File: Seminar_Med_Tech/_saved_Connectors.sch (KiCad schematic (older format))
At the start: 2 parts

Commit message: Updated Dokumentation
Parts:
- added JP?: Jumper_NC_Dual, symbol Jumper_NC_Dual
- added R?: R, symbol R
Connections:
- net SPI_CLK: now reaches J?.13 (P13)
- net EXT_CLK: now reaches J?.15 (P15)
- net GND: now reaches J?.4 (P4)
- net GND: now also J?.2 (P2), JP?.1
- net SPI_START: now reaches J?.1 (P1)
- net /RESET: now reaches J?.10 (P10)
- net SPI_IN: now reaches J?.12 (P12)
- net SPI_OUT: now reaches J?.14 (P14)
- net at J?.18 (P18): now also JP?.3
- net SPI_CS1: now reaches J?.3 (P3)
- net SPI_DRDY: now reaches J?.5 (P5)
- net SPI_CS2: now reaches J?.7 (P7)
- new net CLKSEL: JP?.2, R?.2
- new net DVDD: R?.1
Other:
- moved on the sheet: J?
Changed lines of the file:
@@
 L CONN_02X10 J?
 U 1 1 593AD152
-P 6150 4000
-F 0 "J?" H 6150 4550 50  0000 C CNN
-F 1 "CONN_02X10" V 6150 4000 50  0000 C CNN
-F 2 "" H 6150 2800 50  0001 C CNN
-F 3 "" H 6150 2800 50  0001 C CNN
-	1    6150 4000
+P 6625 4000
+F 0 "J?" H 6625 4550 50  0000 C CNN
+F 1 "CONN_02X10" V 6625 4000 50  0000 C CNN
+F 2 "" H 6625 2800 50  0001 C CNN
+F 3 "" H 6625 2800 50  0001 C CNN
+	1    6625 4000
 	1    0    0    -1
 $EndComp
+Text GLabel 4075 4150 0    60   Input ~ 0
+SPI_CLK
+Text GLabel 7500 4050 2    60   Input ~ 0
+SPI_IN
+Text GLabel 7500 4150 2    60   Input ~ 0
+SPI_OUT
+Text GLabel 7500 3950 2    60   Input ~ 0
+/RESET
+Text GLabel 6050 3650 0    60   Input ~ 0
+SPI_CS1
+Text GLabel 6050 3550 0    60   Input ~ 0
+SPI_START
+Text GLabel 6050 3750 0    60   Input ~ 0
+SPI_DRDY
+Text GLabel 6050 3850 0    60   Input ~ 0
+SPI_CS2
+Text GLabel 4075 4250 0    60   Output ~ 0
+EXT_CLK
+$Comp
+L Jumper_NC_Dual JP?
+U 1 1 593ADF16
+P 8525 4600
+F 0 "JP?" H 8575 4500 50  0000 L CNN
+F 1 "Jumper_NC_Dual" H 8525 4700 50  0000 C BNN
+F 2 "" H 8525 4600 50  0001 C CNN
+F 3 "" H 8525 4600 50  0001 C CNN
+	1    8525 4600
+	0    -1   -1   0
+$EndComp
+Text GLabel 8975 4600 2    60   Input ~ 0
+CLKSEL
+$Comp
+L R R?
+U 1 1 593ADFF6
+P 8800 4225
+F 0 "R?" V 8880 4225 50  0000 C CNN
+F 1 "R" V 8800 4225 50  0000 C CNN
+F 2 "" V 8730 4225 50  0001 C CNN
+F 3 "" H 8800 4225 50  0001 C CNN
+	1    8800 4225
+	1    0    0    -1
+$EndComp
+Text Label 8800 3950 2    60   ~ 0
+DVDD
+$Comp
+L GND #PWR?
+U 1 1 593AE084
+P 8525 4850
+F 0 "#PWR?" H 8525 4600 50  0001 C CNN
+F 1 "GND" H 8525 4700 50  0000 C CNN
+F 2 "" H 8525 4850 50  0001 C CNN
+F 3 "" H 8525 4850 50  0001 C CNN
+	1    8525 4850
+	1    0    0    -1
+$EndComp
+Wire Wire Line
+	4300 4150 4075 4150
+Wire Wire Line
+	7500 4050 6875 4050
+Wire Wire Line
+	6875 4150 7500 4150
+Wire Wire Line
+	6875 3950 7500 3950
+Wire Wire Line
+	6050 3850 6375 3850
+Wire Wire Line
+	6375 3550 6050 3550
+Wire Wire Line
+	6375 3750 6050 3750
+Wire Wire Line
+	6050 3650 6375 3650
+Wire Wire Line
+	4075 4250 4300 4250
+Wire Wire Line
+	6875 4350 8525 4350
+Wire Wire Line
+	8625 4600 8975 4600
+Wire Wire Line
+	8800 4375 8800 4600
+Connection ~ 8800 4600
+Wire Wire Line
+	8800 4075 8800 3950
+Wire Wire Line
+	4800 3650 5175 3650
+Wire Wire Line
+	5175 3650 5175 5000
+$Comp
+L GND #PWR?
+U 1 1 593AE114
+P 5175 5000
+F 0 "#PWR?" H 5175 4750 50  0001 C CNN
+F 1 "GND" H 5175 4850 50  0000 C CNN
+F 2 "" H 5175 5000 50  0001 C CNN
+F 3 "" H 5175 5000 50  0001 C CNN
+	1    5175 5000
+	1    0    0    -1
+$EndComp
+Wire Wire Line
+	6875 3550 6950 3550
+Wire Wire Line
+	6950 3550 6950 3175
+Wire Wire Line
+	6950 3175 9425 3175
+Wire Wire Line
+	9425 3175 9425 3375
+$Comp
+L GND #PWR?
+U 1 1 593AE149
+P 9425 3375
+F 0 "#PWR?" H 9425 3125 50  0001 C CNN
+F 1 "GND" H 9425 3225 50  0000 C CNN
+F 2 "" H 9425 3375 50  0001 C CNN
+F 3 "" H 9425 3375 50  0001 C CNN
+	1    9425 3375
+	1    0    0    -1
+$EndComp

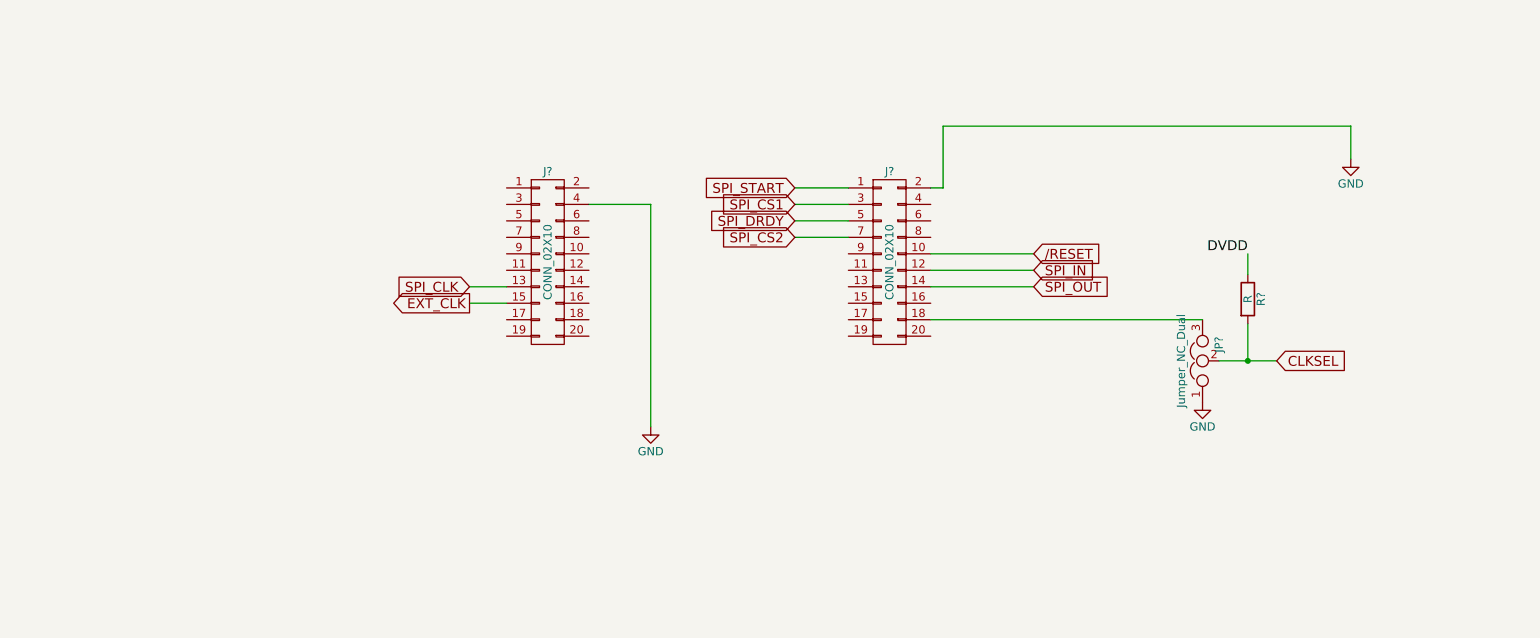
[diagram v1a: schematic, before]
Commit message: Updated Dokumentation and connectors
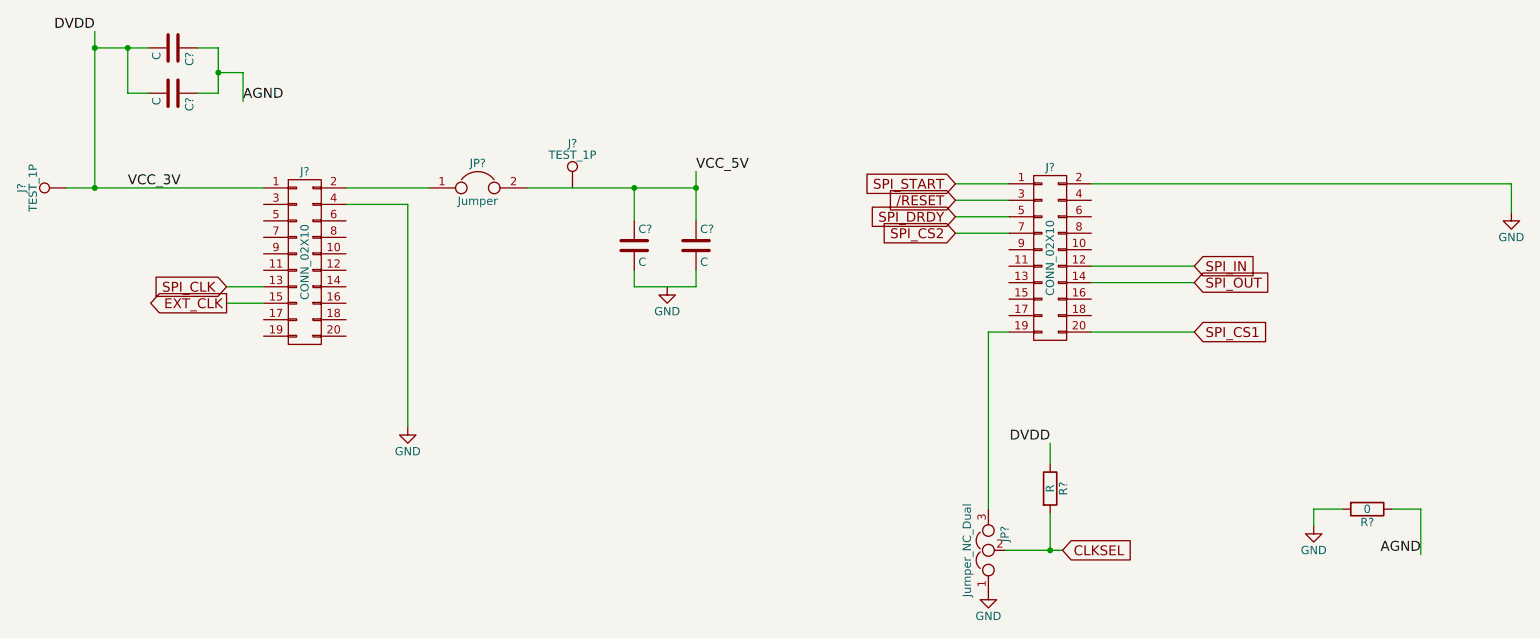
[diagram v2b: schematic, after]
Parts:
- added C? (x4): C, symbol C
- added J? (x2): TEST_1P, symbol TEST_1P
- added JP?: Jumper, symbol Jumper
- added R?: 0, symbol R
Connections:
- net /RESET: now also J?.3 (P3); no longer J?.10 (P10)
- net DVDD: now also J?.1 (P1), C?.2, C?.2, J?.1
- net GND: now also R?.2
- net SPI_CS1: now also J?.20 (P20); no longer J?.3 (P3)
- net at J?.2 (P2): now also JP?.1
- net at J?.18 (P18): no longer JP?.3
- net at J?.19 (P19): now also JP?.3
- new net: C?.2, C?.2
- new net AGND: C?.1, C?.1, R?.1
- new net VCC_5V: C?.1, C?.1, JP?.2
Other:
- moved on the sheet: J?, JP?, R?
